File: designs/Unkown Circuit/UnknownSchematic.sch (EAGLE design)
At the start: 47 parts, among them IC1 REG1118, IC2 PIC16F1517/19PT, U1 0914-0-15-20-77-14-11-0

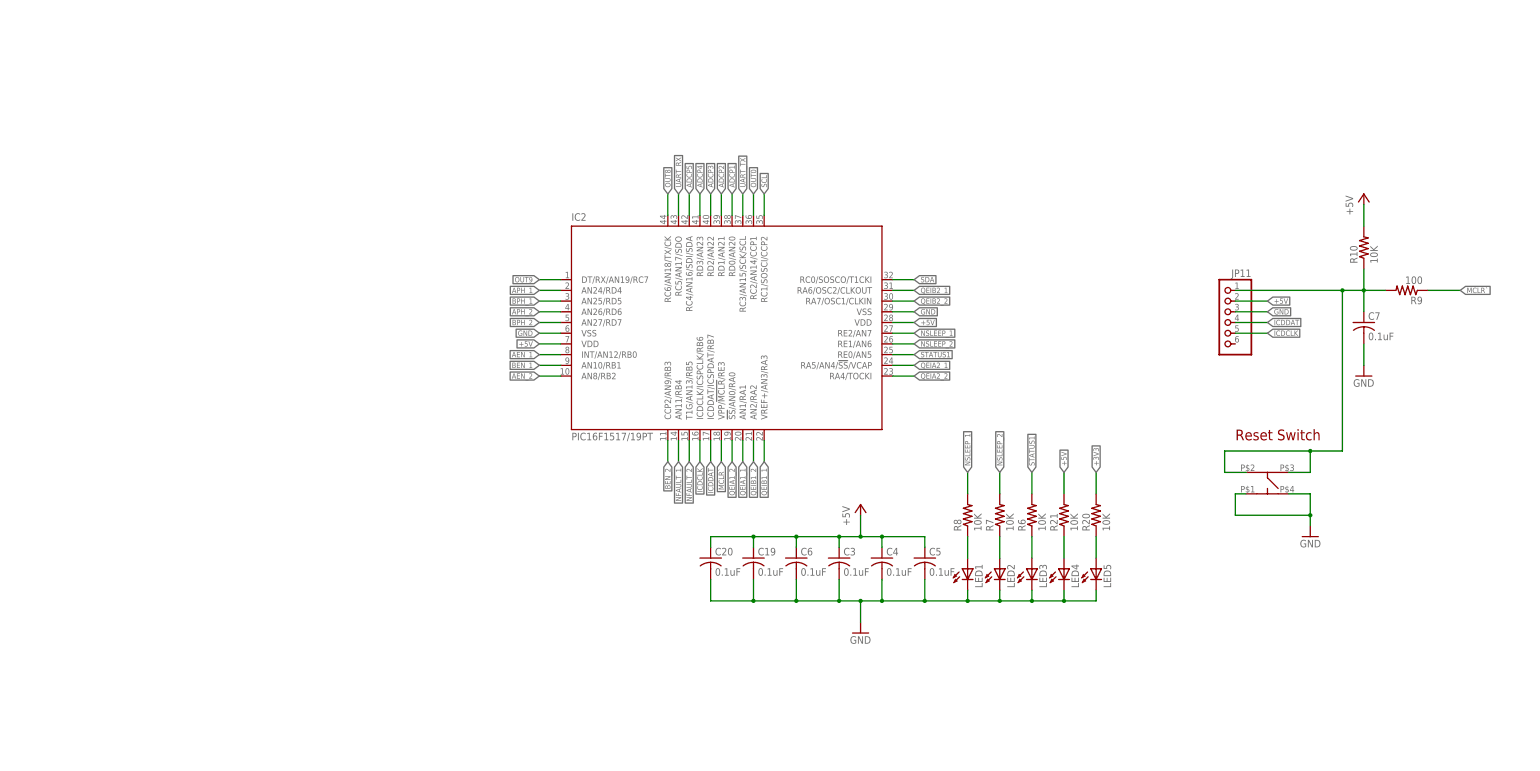
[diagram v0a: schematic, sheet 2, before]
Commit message: Updated Unknown Circuit Schematic
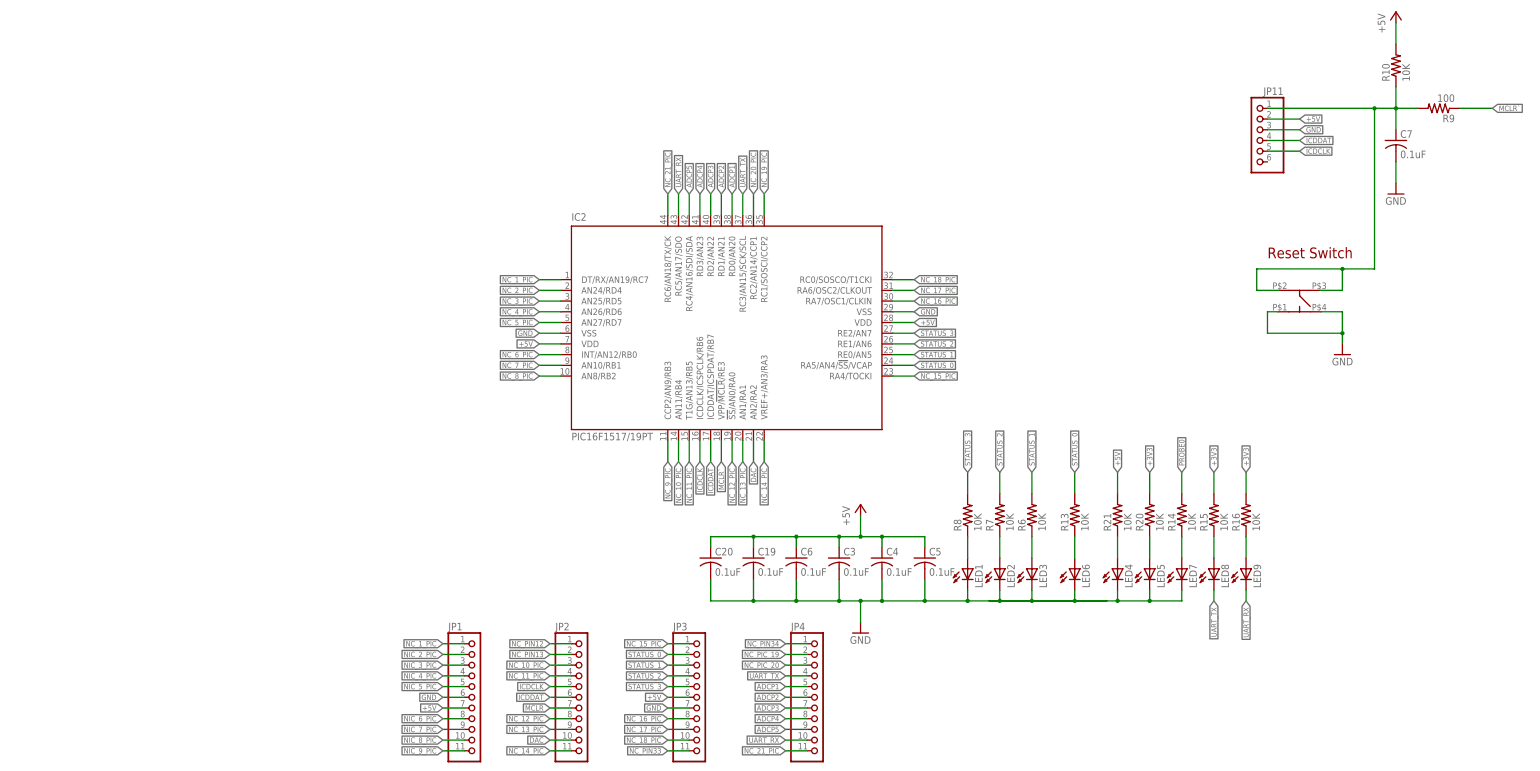
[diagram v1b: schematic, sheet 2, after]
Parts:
- added C10: 1 uF, rcl:C-USC0805
- added C11: 4.7 uF, rcl:C-USC0805
- added C8, C9: 0.01 uF, rcl:C-USC0805
- added IC3: LF442D, linear:LF442D
- added IC4: REG1118, burr-brown:REG1118
- added JP2, JP3, JP4: (no value), pinhead:PINHD-1X11
- added JP5: (no value), pinhead:PINHD-1X2
- added LED6, LED7, LED8, LED9: (no value), interface_board-rev13:LEDSML0603
- added R11, R12: 4.7k, rcl:R-US_R0805
- added R13, R14, R15, R16: 10K, rcl:R-US_R1206
- JP1: device pinhead:PINHD-1X8 -> pinhead:PINHD-1X11
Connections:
- net AEN_1 renamed NC_6_PIC
- net AEN_2 renamed NC_8_PIC
- net APH_1 renamed NC_2_PIC
- net APH_2 renamed NC_4_PIC
- net BEN_1 renamed NC_7_PIC
- net BEN_2 renamed NC_9_PIC
- net BPH_1 renamed NC_3_PIC
- net BPH_2 renamed NC_5_PIC
- net OUT0 renamed NC_20_PIC
- net SCL renamed NC_19_PIC
- removed net +3V3_KB: BT_FTDI.REGIN, BT_FTDI.VDD, C37.2, C38.2, C39.2, C40.2, R46.2
- removed net NFAULT_1: IC2.AN11/RB4
- removed net NFAULT_2: IC2.T1G/AN13/RB5
- removed net NSLEEP_1: IC2.RE2/AN7, R8.2
- removed net NSLEEP_2: IC2.RE1/AN6, R7.2
- removed net OUT8: IC2.RC6/AN18/TX/CK
- removed net OUT9: IC2.DT/RX/AN19/RC7
- removed net QEIA1_1: IC2.AN1/RA1
- removed net QEIA1_2: IC2.!SS!/AN0/RA0
- removed net QEIA2_1: IC2.RA5/AN4/!SS!/VCAP
- removed net QEIA2_2: IC2.RA4/TOCKI
- removed net QEIB1_1: IC2.VREF+/AN3/RA3
- removed net QEIB1_2: IC2.AN2/RA2
- removed net QEIB2_1: IC2.RA6/OSC2/CLKOUT
- removed net QEIB2_2: IC2.RA7/OSC1/CLKIN
- removed net SDA: IC2.RC0/SOSCO/T1CKI
- removed net STATUS1: IC2.RE0/AN5, R6.2
- new net GND1: LED6.C
- new net N$10: LED8.A, R15.1
- new net N$11: LED9.A, R16.1
- new net N$2: IC3B.-IN, R11.2, R12.1
- new net N$3: LED6.A, R13.1
- new net N$4: LED7.A, R14.1
- new net NC_10_PIC: IC2.AN11/RB4, JP2.3
- new net NC_11_PIC: IC2.T1G/AN13/RB5, JP2.4
- new net NC_12_PIC: IC2.!SS!/AN0/RA0, JP2.8
- new net NC_13_PIC: IC2.AN1/RA1, JP2.9
- new net NC_14_PIC: IC2.VREF+/AN3/RA3, JP2.11
- new net NC_15_PIC: IC2.RA4/TOCKI, JP3.1
- new net NC_16_PIC: IC2.RA7/OSC1/CLKIN, JP3.8
- new net NC_17_PIC: IC2.RA6/OSC2/CLKOUT, JP3.9
- new net NC_18_PIC: IC2.RC0/SOSCO/T1CKI, JP3.10
- new net NC_1_PIC: IC2.DT/RX/AN19/RC7, JP1.1
- new net NC_21_PIC: IC2.RC6/AN18/TX/CK, JP4.11
- new net NC_PIC_19: JP4.2
- new net NC_PIC_20: JP4.3
- new net NC_PIN12: JP2.1
- new net NC_PIN13: JP2.2
- new net NC_PIN33: JP3.11
- new net NC_PIN34: JP4.1
- new net NIC_2_PIC: JP1.2
- new net NIC_3_PIC: JP1.3
- new net NIC_4_PIC: JP1.4
- new net NIC_5_PIC: JP1.5
- new net NIC_6_PIC: JP1.8
- new net NIC_7_PIC: JP1.9
- new net NIC_8_PIC: JP1.10
- new net NIC_9_PIC: JP1.11
- new net STATUS_0: IC2.RA5/AN4/!SS!/VCAP, JP3.2, R13.2
- new net STATUS_1: IC2.RE0/AN5, JP3.3, R6.2
- new net STATUS_2: IC2.RE1/AN6, JP3.4, R7.2
- new net STATUS_3: IC2.RE2/AN7, JP3.5, R8.2
- net +3V3: now also BT_FTDI.REGIN, BT_FTDI.VDD, C10.1, C37.2, C38.2, C39.2, C40.2, IC4.VOUT, R15.2, R16.2, R46.2
- net +5V: now also C11.1, IC3P.V+, IC4.VIN, JP1.7, JP3.6; no longer JP1.1
- net ADCP1: now also JP4.5; no longer JP1.3
- net ADCP2: now also JP4.6; no longer JP1.4
- net ADCP3: now also JP4.7; no longer JP1.5
- net ADCP4: now also JP4.8; no longer JP1.6
- net ADCP5: now also JP4.9; no longer JP1.7
- net BUFFEROUTPUT: now also C9.1, IC3B.OUT, JP5.2, R11.1
- net DAC: now also C8.2, IC2.AN2/RA2, IC3B.+IN, JP2.10, JP5.1; no longer JP1.2
- net GND: now also C10.2, C11.2, C8.1, C9.2, IC3P.V-, IC4.GND, JP1.6, JP3.7, LED7.C, R12.2; no longer JP1.8
- net ICDCLK: now also JP2.5
- net ICDDAT: now also JP2.6
- net MCLR: now also JP2.7
- net PROBE0: now also R14.2
- net UART_RX: now also JP4.10, LED9.C
- net UART_TX: now also JP4.4, LED8.C
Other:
- moved on the sheet: C7, JP11, LED4, LED5, R10, R20, R21, R9

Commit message: Fiexd +5 V
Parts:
- removed BT_USB_MICROB: USB-MICROB, Mother-Board-rev5:USB-MICROB
- removed C3, C4, C5: 0.1uF, rcl:C-USC0805
- removed FTDI: (no value), interface_board-rev13:LEDCHIPLED_1206
- removed IC3: LF442D, linear:LF442D
- removed JP3, JP4: (no value), pinhead:PINHD-1X11
- added H1, H10, H2, H3, H4, H5, H6, H7, H8, H9: MOUNT-PAD-ROUND3.2, holes:MOUNT-PAD-ROUND3.2
- added IC5: UA741D, linear:UA741D
- added LED10: (no value), interface_board-rev13:LEDSML0603
- JP2: device pinhead:PINHD-1X11 -> pinhead:PINHD-1X4
- R47: value 330 -> 500
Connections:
- removed net BT_VBUS: BT_FTDI.VBUS, BT_USB_MICROB.VBUS, R47.2
- removed net NC_PIC_19: JP4.2
- removed net NC_PIC_20: JP4.3
- removed net NC_PIN12: JP2.1
- removed net NC_PIN13: JP2.2
- removed net NC_PIN33: JP3.11
- removed net NC_PIN34: JP4.1
- removed net NIC_2_PIC: JP1.2
- removed net NIC_3_PIC: JP1.3
- removed net NIC_4_PIC: JP1.4
- removed net NIC_5_PIC: JP1.5
- removed net NIC_6_PIC: JP1.8
- removed net NIC_7_PIC: JP1.9
- removed net NIC_8_PIC: JP1.10
- removed net NIC_9_PIC: JP1.11
- net +5V: now also BT_FTDI.VBUS, IC5.V+, JP2.2, R47.2; no longer C3.1, C4.1, C5.1, IC3P.V+, JP1.7, JP3.6
- net ADCP1: no longer JP4.5
- net ADCP2: no longer JP4.6
- net ADCP3: no longer JP4.7
- net ADCP4: no longer JP4.8
- net ADCP5: no longer JP4.9
- net BT_D+: now also JP2.4; no longer BT_USB_MICROB.D+
- net BT_D-: now also JP2.3; no longer BT_USB_MICROB.D-
- net BUFFEROUTPUT: now also IC5.OUT; no longer IC3B.OUT
- net DAC: now also IC5.+IN; no longer IC3B.+IN, JP2.10
- net GND: now also IC5.V-, JP2.1, LED10.C; no longer BT_USB_MICROB.GND, C3.2, C4.2, C5.2, FTDI.C, IC3P.V-, JP1.6, JP3.7
- net ICDCLK: no longer JP2.5
- net ICDDAT: no longer JP2.6
- net MCLR: no longer JP2.7
- net N$2: now also IC5.-IN; no longer IC3B.-IN
- net N$9: now also LED10.A; no longer FTDI.A
- net NC_10_PIC: no longer JP2.3
- net NC_11_PIC: no longer JP2.4
- net NC_12_PIC: no longer JP2.8
- net NC_13_PIC: no longer JP2.9
- net NC_14_PIC: no longer JP2.11
- net NC_15_PIC: no longer JP3.1
- net NC_16_PIC: no longer JP3.8
- net NC_17_PIC: no longer JP3.9
- net NC_18_PIC: no longer JP3.10
- net NC_1_PIC: no longer JP1.1
- net NC_21_PIC: no longer JP4.11
- net STATUS_0: no longer JP3.2
- net STATUS_1: no longer JP3.3
- net STATUS_2: no longer JP3.4
- net STATUS_3: no longer JP3.5
- net UART_RX: no longer JP4.10
- net UART_TX: no longer JP4.4
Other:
- moved on the sheet: JP1

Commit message: Done with Unknow circuit
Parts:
- removed JP1: (no value), pinhead:PINHD-1X11
- IC1: value REG1118 -> +2.5v
- IC4: value REG1118 -> +3.3v
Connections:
- removed net GND1: LED6.C
- net ADCP1: now also IC2.RC4/AN16/SDI/SDA; no longer IC2.RD0/AN20
- net ADCP2: now also IC2.RD3/AN23; no longer IC2.RD1/AN21
- net ADCP4: now also IC2.RD0/AN20; no longer IC2.RD3/AN23
- net ADCP5: now also IC2.RD1/AN21; no longer IC2.RC4/AN16/SDI/SDA
- net GND: now also H1.MOUNT, H10.MOUNT, H2.MOUNT, H3.MOUNT, H4.MOUNT, H5.MOUNT, H6.MOUNT, H7.MOUNT, H8.MOUNT, H9.MOUNT, LED6.C

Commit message: done with first version of the boards
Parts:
- added R17: 100, rcl:R-US_R0805
- added R18: 10K, rcl:R-US_R0805
- added U$1: LOGO, IEEE-logo:LOGO
- added U2: QRE11131:1, Testing:QRE11131:1
- IC1, IC4: device burr-brown:REG1118 -> burr-brown:REG1117
- R13, R14, R15, R16, R20, R21, R6, R7, R8: device rcl:R-US_R1206 -> rcl:R-US_R0805
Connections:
- removed net NC_20_PIC: IC2.RC2/AN14/CCP1
- new net IR_RANGE: IC2.RC2/AN14/CCP1, R18.2, U2.C
- new net N$12: R17.1, U2.A
- net +5V: now also R17.2, R18.1
- net GND: now also U2.E, U2.K
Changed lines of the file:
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@@
 <part name="U1" library="Stage1ProbeMount" deviceset="STAGE1PROBEMOUNT" device="" value="0914-0-15-20-77-14-11-0"/>
 <part name="D1" library="diode" deviceset="DIODE-" device="DO214AA" value="STPS1L30U "/>
-<part name="IC1" library="burr-brown" deviceset="REG1118" device="" value="+2.5v"/>
+<part name="IC1" library="burr-brown" deviceset="REG1117" device="" value="+2.5v"/>
 <part name="GND1" library="supply1" deviceset="GND" device=""/>
 <part name="C1" library="rcl" deviceset="C-US" device="C0805" value="1 uF"/>
@@
 <part name="LED2" library="interface_board-rev13" deviceset="LED" device="SML0603"/>
 <part name="LED3" library="interface_board-rev13" deviceset="LED" device="SML0603"/>
-<part name="R6" library="rcl" deviceset="R-US_" device="R1206" value="10K"/>
-<part name="R7" library="rcl" deviceset="R-US_" device="R1206" value="10K"/>
-<part name="R8" library="rcl" deviceset="R-US_" device="R1206" value="10K"/>
+<part name="R6" library="rcl" deviceset="R-US_" device="R0805" value="10K"/>
+<part name="R7" library="rcl" deviceset="R-US_" device="R0805" value="10K"/>
+<part name="R8" library="rcl" deviceset="R-US_" device="R0805" value="10K"/>
 <part name="C6" library="rcl" deviceset="C-US" device="C0805" value="0.1uF"/>
 <part name="C19" library="rcl" deviceset="C-US" device="C0805" value="0.1uF"/>
@@
 <part name="LED4" library="interface_board-rev13" deviceset="LED" device="SML0603"/>
 <part name="LED5" library="interface_board-rev13" deviceset="LED" device="SML0603"/>
-<part name="R20" library="rcl" deviceset="R-US_" device="R1206" value="10K"/>
-<part name="R21" library="rcl" deviceset="R-US_" device="R1206" value="10K"/>
+<part name="R20" library="rcl" deviceset="R-US_" device="R0805" value="10K"/>
+<part name="R21" library="rcl" deviceset="R-US_" device="R0805" value="10K"/>
 <part name="JP11" library="pinhead" deviceset="PINHD-1X6" device="/90"/>
 <part name="R9" library="rcl" deviceset="R-US_" device="R1206" value="100"/>
@@
 <part name="C8" library="rcl" deviceset="C-US" device="C0805" value="0.01 uF"/>
 <part name="C9" library="rcl" deviceset="C-US" device="C0805" value="0.01 uF"/>
-<part name="IC4" library="burr-brown" deviceset="REG1118" device="" value="+3.3v"/>
+<part name="IC4" library="burr-brown" deviceset="REG1117" device="" value="+3.3v"/>
 <part name="GND3" library="supply1" deviceset="GND" device=""/>
 <part name="C10" library="rcl" deviceset="C-US" device="C0805" value="1 uF"/>
 <part name="C11" library="rcl" deviceset="C-US" device="C0805" value="4.7 uF"/>
 <part name="LED6" library="interface_board-rev13" deviceset="LED" device="SML0603"/>
-<part name="R13" library="rcl" deviceset="R-US_" device="R1206" value="10K"/>
+<part name="R13" library="rcl" deviceset="R-US_" device="R0805" value="10K"/>
 <part name="LED7" library="interface_board-rev13" deviceset="LED" device="SML0603"/>
-<part name="R14" library="rcl" deviceset="R-US_" device="R1206" value="10K"/>
+<part name="R14" library="rcl" deviceset="R-US_" device="R0805" value="10K"/>
 <part name="LED8" library="interface_board-rev13" deviceset="LED" device="SML0603"/>
-<part name="R15" library="rcl" deviceset="R-US_" device="R1206" value="10K"/>
+<part name="R15" library="rcl" deviceset="R-US_" device="R0805" value="10K"/>
 <part name="LED9" library="interface_board-rev13" deviceset="LED" device="SML0603"/>
-<part name="R16" library="rcl" deviceset="R-US_" device="R1206" value="10K"/>
+<part name="R16" library="rcl" deviceset="R-US_" device="R0805" value="10K"/>
 <part name="JP5" library="pinhead" deviceset="PINHD-1X2" device=""/>
 <part name="H1" library="holes" deviceset="MOUNT-PAD-ROUND" device="3.2"/>
@@
 <part name="JP2" library="pinhead" deviceset="PINHD-1X4" device=""/>
 <part name="GND4" library="supply1" deviceset="GND" device=""/>
+<part name="R17" library="rcl" deviceset="R-US_" device="R0805" value="100"/>
+<part name="R18" library="rcl" deviceset="R-US_" device="R0805" value="10K"/>
+<part name="U2" library="Testing" deviceset="QRE1113" device="1:1"/>
+<part name="GND5" library="SparkFun" deviceset="GND" device=""/>
+<part name="GND6" library="SparkFun" deviceset="GND" device=""/>
+<part name="U$1" library="IEEE-logo" deviceset="LOGO" device=""/>
 </parts>
 <sheets>
@@
 <instance part="IC5" gate="A" x="223.52" y="162.56"/>
 <instance part="GND4" gate="1" x="40.64" y="10.16"/>
+<instance part="R17" gate="G$1" x="124.46" y="58.42" smashed="yes" rot="R90">
+<attribute name="NAME" x="122.936" y="55.118" size="1.778" layer="95" rot="R90"/>
+<attribute name="VALUE" x="127.762" y="58.42" size="1.778" layer="96" rot="R90"/>
+</instance>
+<instance part="R18" gate="G$1" x="132.08" y="58.42" smashed="yes" rot="R270">
+<attribute name="NAME" x="130.556" y="55.118" size="1.778" layer="95" rot="R90"/>
+<attribute name="VALUE" x="135.128" y="59.182" size="1.778" layer="96" rot="R90"/>
+</instance>
+<instance part="U2" gate="G$1" x="129.54" y="43.18" smashed="yes" rot="MR0">
+<attribute name="NAME" x="133.35" y="46.482" size="1.778" layer="95"/>
+<attribute name="VALUE" x="133.096" y="35.56" size="1.778" layer="96"/>
+</instance>
+<instance part="GND5" gate="1" x="124.46" y="30.48"/>
+<instance part="GND6" gate="1" x="132.08" y="30.48"/>
+<instance part="U$1" gate="G$1" x="220.98" y="53.34"/>
 </instances>
 <busses>
@@
 <junction x="40.64" y="20.32"/>
 </segment>
+<segment>
+<wire x1="124.46" y1="33.02" x2="124.46" y2="35.56" width="0.1524" layer="91"/>
+<pinref part="U2" gate="G$1" pin="K"/>
+<pinref part="GND5" gate="1" pin="GND"/>
+</segment>
+<segment>
+<wire x1="132.08" y1="35.56" x2="132.08" y2="33.02" width="0.1524" layer="91"/>
+<pinref part="U2" gate="G$1" pin="E"/>
+<pinref part="GND6" gate="1" pin="GND"/>
+</segment>
 </net>
 <net name="+5V" class="0">
@@
 <pinref part="IC5" gate="A" pin="V+"/>
 <label x="220.98" y="172.72" size="1.27" layer="95" rot="R180" xref="yes"/>
+</segment>
+<segment>
+<pinref part="R17" gate="G$1" pin="2"/>
+<wire x1="124.46" y1="63.5" x2="124.46" y2="66.04" width="0.1524" layer="91"/>
+<pinref part="R18" gate="G$1" pin="1"/>
+<wire x1="124.46" y1="66.04" x2="129.54" y2="66.04" width="0.1524" layer="91"/>
+<wire x1="129.54" y1="66.04" x2="132.08" y2="66.04" width="0.1524" layer="91"/>
+<wire x1="132.08" y1="66.04" x2="132.08" y2="63.5" width="0.1524" layer="91"/>
+<wire x1="129.54" y1="66.04" x2="129.54" y2="68.58" width="0.1524" layer="91"/>
+<junction x="129.54" y="66.04"/>
+<label x="129.54" y="68.58" size="1.778" layer="95" rot="R90" xref="yes"/>
 </segment>
 </net>
@@
 <wire x1="218.44" y1="106.68" x2="220.98" y2="106.68" width="0.1524" layer="91"/>
 <label x="220.98" y="106.68" size="1.27" layer="95" xref="yes"/>
+</segment>
+</net>
+<net name="N$12" class="0">
+<segment>
+<wire x1="124.46" y1="53.34" x2="124.46" y2="48.26" width="0.1524" layer="91"/>
+<pinref part="R17" gate="G$1" pin="1"/>
+<pinref part="U2" gate="G$1" pin="A"/>
+</segment>
+</net>
+<net name="IR_RANGE" class="0">
+<segment>
+<wire x1="132.08" y1="48.26" x2="132.08" y2="50.8" width="0.1524" layer="91"/>
+<pinref part="R18" gate="G$1" pin="2"/>
+<pinref part="U2" gate="G$1" pin="C"/>
+<wire x1="132.08" y1="50.8" x2="132.08" y2="53.34" width="0.1524" layer="91"/>
+<wire x1="132.08" y1="50.8" x2="142.24" y2="50.8" width="0.1524" layer="91"/>
+<junction x="132.08" y="50.8"/>
+<label x="142.24" y="50.8" size="1.778" layer="95" xref="yes"/>
 </segment>
 </net>
@@
 </segment>
 </net>
-<net name="NC_20_PIC" class="0">
+<net name="IR_RANGE" class="0">
 <segment>
 <wire x1="86.36" y1="160.02" x2="86.36" y2="165.1" width="0.1524" layer="91"/>
